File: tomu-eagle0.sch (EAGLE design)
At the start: 18 parts, among them U1 EFM32HG309F64G

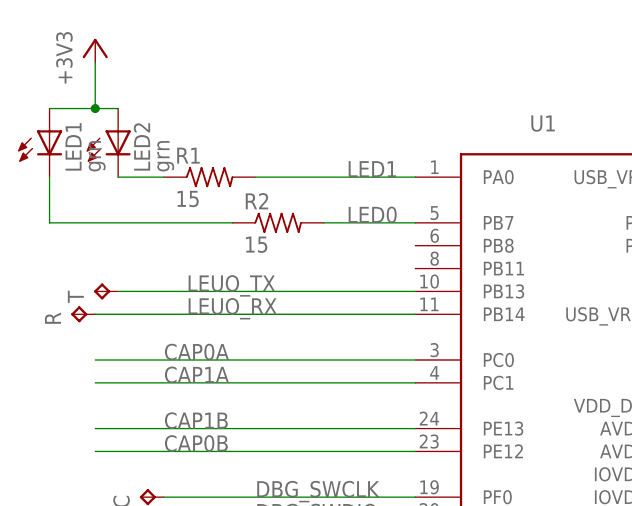
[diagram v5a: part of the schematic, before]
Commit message: LED resistors should be 75 not 15 (or maybe 52 as in the tomu bom)
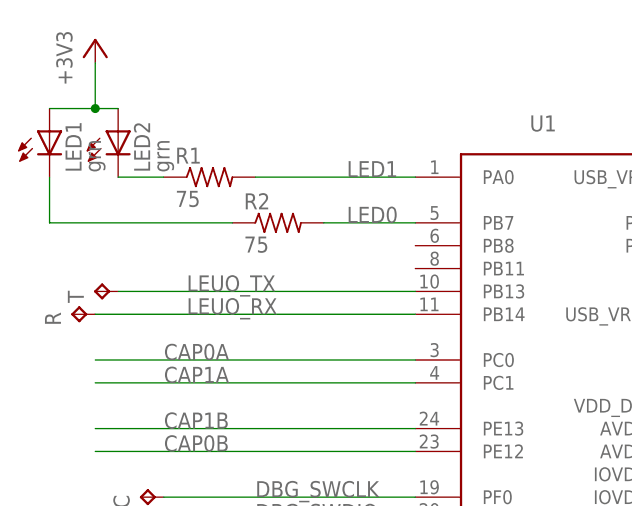
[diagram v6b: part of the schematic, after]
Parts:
- R1, R2: value 15 -> 75
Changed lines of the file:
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@@
 <?xml version="1.0" encoding="utf-8"?>
 <!DOCTYPE eagle SYSTEM "eagle.dtd">
-<eagle version="8.6.0">
+<eagle version="8.7.1">
 <drawing>
 <settings>
@@
 <grid distance="0.1" unitdist="inch" unit="inch" style="lines" multiple="1" display="no" altdistance="0.01" altunitdist="inch" altunit="inch"/>
 <layers>
-<layer number="1" name="Top" color="4" fill="1" visible="yes" active="no"/>
-<layer number="2" name="Route2" color="1" fill="3" visible="yes" active="no"/>
-<layer number="3" name="Route3" color="4" fill="3" visible="yes" active="no"/>
-<layer number="4" name="Route4" color="1" fill="4" visible="yes" active="no"/>
-<layer number="5" name="Route5" color="4" fill="4" visible="yes" active="no"/>
-<layer number="6" name="Route6" color="1" fill="8" visible="yes" active="no"/>
-<layer number="7" name="Route7" color="4" fill="8" visible="yes" active="no"/>
-<layer number="8" name="Route8" color="1" fill="2" visible="yes" active="no"/>
-<layer number="9" name="Route9" color="4" fill="2" visible="yes" active="no"/>
-<layer number="10" name="Route10" color="1" fill="7" visible="yes" active="no"/>
-<layer number="11" name="Route11" color="4" fill="7" visible="yes" active="no"/>
-<layer number="12" name="Route12" color="1" fill="5" visible="yes" active="no"/>
-<layer number="13" name="Route13" color="4" fill="5" visible="yes" active="no"/>
-<layer number="14" name="Route14" color="1" fill="6" visible="yes" active="no"/>
-<layer number="15" name="Route15" color="4" fill="6" visible="yes" active="no"/>
-<layer number="16" name="Bottom" color="3" fill="1" visible="yes" active="no"/>
-<layer number="17" name="Pads" color="2" fill="1" visible="yes" active="no"/>
-<layer number="18" name="Vias" color="2" fill="1" visible="yes" active="no"/>
-<layer number="19" name="Unrouted" color="6" fill="1" visible="yes" active="no"/>
-<layer number="20" name="Dimension" color="15" fill="1" visible="yes" active="no"/>
-<layer number="21" name="tPlace" color="7" fill="1" visible="yes" active="no"/>
-<layer number="22" name="bPlace" color="7" fill="1" visible="yes" active="no"/>
-<layer number="23" name="tOrigins" color="15" fill="1" visible="yes" active="no"/>
-<layer number="24" name="bOrigins" color="15" fill="1" visible="yes" active="no"/>
-<layer number="25" name="tNames" color="7" fill="1" visible="yes" active="no"/>
-<layer number="26" name="bNames" color="7" fill="1" visible="yes" active="no"/>
-<layer number="27" name="tValues" color="7" fill="1" visible="yes" active="no"/>
-<layer number="28" name="bValues" color="7" fill="1" visible="yes" active="no"/>
+<layer number="1" name="Top" color="4" fill="1" visible="no" active="no"/>
+<layer number="2" name="Route2" color="1" fill="3" visible="no" active="no"/>
+<layer number="3" name="Route3" color="4" fill="3" visible="no" active="no"/>
+<layer number="4" name="Route4" color="1" fill="4" visible="no" active="no"/>
+<layer number="5" name="Route5" color="4" fill="4" visible="no" active="no"/>
+<layer number="6" name="Route6" color="1" fill="8" visible="no" active="no"/>
+<layer number="7" name="Route7" color="4" fill="8" visible="no" active="no"/>
+<layer number="8" name="Route8" color="1" fill="2" visible="no" active="no"/>
+<layer number="9" name="Route9" color="4" fill="2" visible="no" active="no"/>
+<layer number="10" name="Route10" color="1" fill="7" visible="no" active="no"/>
+<layer number="11" name="Route11" color="4" fill="7" visible="no" active="no"/>
+<layer number="12" name="Route12" color="1" fill="5" visible="no" active="no"/>
+<layer number="13" name="Route13" color="4" fill="5" visible="no" active="no"/>
+<layer number="14" name="Route14" color="1" fill="6" visible="no" active="no"/>
+<layer number="15" name="Route15" color="4" fill="6" visible="no" active="no"/>
+<layer number="16" name="Bottom" color="3" fill="1" visible="no" active="no"/>
+<layer number="17" name="Pads" color="2" fill="1" visible="no" active="no"/>
+<layer number="18" name="Vias" color="2" fill="1" visible="no" active="no"/>
+<layer number="19" name="Unrouted" color="6" fill="1" visible="no" active="no"/>
+<layer number="20" name="Dimension" color="15" fill="1" visible="no" active="no"/>
+<layer number="21" name="tPlace" color="7" fill="1" visible="no" active="no"/>
+<layer number="22" name="bPlace" color="7" fill="1" visible="no" active="no"/>
+<layer number="23" name="tOrigins" color="15" fill="1" visible="no" active="no"/>
+<layer number="24" name="bOrigins" color="15" fill="1" visible="no" active="no"/>
+<layer number="25" name="tNames" color="7" fill="1" visible="no" active="no"/>
+<layer number="26" name="bNames" color="7" fill="1" visible="no" active="no"/>
+<layer number="27" name="tValues" color="7" fill="1" visible="no" active="no"/>
+<layer number="28" name="bValues" color="7" fill="1" visible="no" active="no"/>
 <layer number="29" name="tStop" color="7" fill="3" visible="no" active="no"/>
 <layer number="30" name="bStop" color="7" fill="6" visible="no" active="no"/>
@@
 <layer number="35" name="tGlue" color="7" fill="4" visible="no" active="no"/>
 <layer number="36" name="bGlue" color="7" fill="5" visible="no" active="no"/>
-<layer number="37" name="tTest" color="7" fill="1" visible="yes" active="no"/>
-<layer number="38" name="bTest" color="7" fill="1" visible="yes" active="no"/>
+<layer number="37" name="tTest" color="7" fill="1" visible="no" active="no"/>
+<layer number="38" name="bTest" color="7" fill="1" visible="no" active="no"/>
 <layer number="39" name="tKeepout" color="4" fill="11" visible="no" active="no"/>
 <layer number="40" name="bKeepout" color="1" fill="11" visible="no" active="no"/>
@@
 <layer number="44" name="Drills" color="7" fill="1" visible="no" active="no"/>
 <layer number="45" name="Holes" color="7" fill="1" visible="no" active="no"/>
-<layer number="46" name="Milling" color="3" fill="1" visible="yes" active="no"/>
-<layer number="47" name="Measures" color="7" fill="1" visible="yes" active="no"/>
-<layer number="48" name="Document" color="7" fill="1" visible="yes" active="no"/>
-<layer number="49" name="Reference" color="7" fill="1" visible="yes" active="no"/>
-<layer number="50" name="dxf" color="7" fill="1" visible="yes" active="no"/>
-<layer number="51" name="tDocu" color="7" fill="1" visible="yes" active="no"/>
-<layer number="52" name="bDocu" color="7" fill="1" visible="yes" active="no"/>
-<layer number="53" name="tGND_GNDA" color="7" fill="9" visible="yes" active="no"/>
-<layer number="54" name="bGND_GNDA" color="1" fill="9" visible="yes" active="no"/>
-<layer number="56" name="wert" color="7" fill="1" visible="yes" active="no"/>
-<layer number="57" name="tCAD" color="7" fill="1" visible="yes" active="no"/>
-<layer number="59" name="tCarbon" color="7" fill="1" visible="yes" active="no"/>
-<layer number="60" name="bCarbon" color="7" fill="1" visible="yes" active="no"/>
+<layer number="46" name="Milling" color="3" fill="1" visible="no" active="no"/>
+<layer number="47" name="Measures" color="7" fill="1" visible="no" active="no"/>
+<layer number="48" name="Document" color="7" fill="1" visible="no" active="no"/>
+<layer number="49" name="Reference" color="7" fill="1" visible="no" active="no"/>
+<layer number="50" name="dxf" color="7" fill="1" visible="no" active="no"/>
+<layer number="51" name="tDocu" color="7" fill="1" visible="no" active="no"/>
+<layer number="52" name="bDocu" color="7" fill="1" visible="no" active="no"/>
+<layer number="53" name="tGND_GNDA" color="7" fill="9" visible="no" active="no"/>
+<layer number="54" name="bGND_GNDA" color="1" fill="9" visible="no" active="no"/>
+<layer number="56" name="wert" color="7" fill="1" visible="no" active="no"/>
+<layer number="57" name="tCAD" color="7" fill="1" visible="no" active="no"/>
+<layer number="59" name="tCarbon" color="7" fill="1" visible="no" active="no"/>
+<layer number="60" name="bCarbon" color="7" fill="1" visible="no" active="no"/>
 <layer number="88" name="SimResults" color="9" fill="1" visible="yes" active="yes"/>
 <layer number="89" name="SimProbes" color="9" fill="1" visible="yes" active="yes"/>
@@
 <part name="GND3" library="supply1" library_urn="urn:adsk.eagle:library:371" deviceset="GND" device=""/>
 <part name="+3V2" library="supply1" library_urn="urn:adsk.eagle:library:371" deviceset="+3V3" device=""/>
-<part name="R1" library="adafruit" library_urn="urn:adsk.eagle:library:420" deviceset="R-US_" device="R0402" value="15"/>
-<part name="R2" library="adafruit" library_urn="urn:adsk.eagle:library:420" deviceset="R-US_" device="R0402" value="15"/>
+<part name="R1" library="adafruit" library_urn="urn:adsk.eagle:library:420" deviceset="R-US_" device="R0402" value="75"/>
+<part name="R2" library="adafruit" library_urn="urn:adsk.eagle:library:420" deviceset="R-US_" device="R0402" value="75"/>
 <part name="LED1" library="adafruit" library_urn="urn:adsk.eagle:library:420" deviceset="LED" device="CHIP-LED0603" value="grn"/>
 <part name="LED2" library="adafruit" library_urn="urn:adsk.eagle:library:420" deviceset="LED" device="CHIP-LED0603" value="grn"/>
